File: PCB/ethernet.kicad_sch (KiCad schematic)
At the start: 32 parts, among them IC24 ENC28J60-I_SO, J6 74990101241, Y1 25MHz

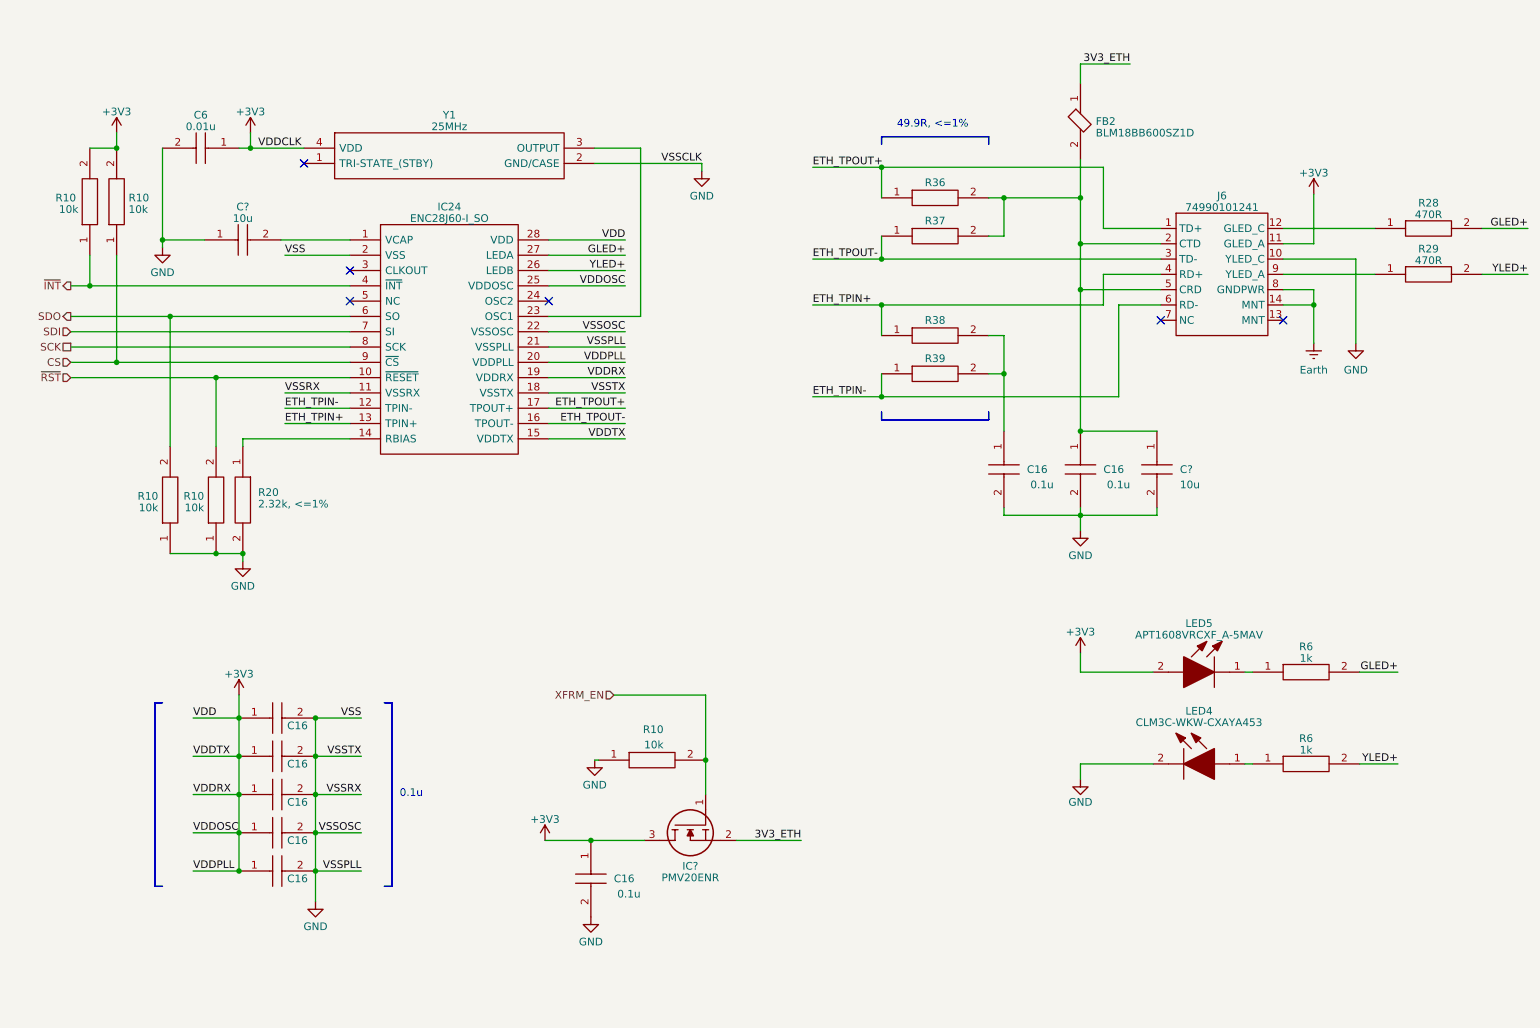
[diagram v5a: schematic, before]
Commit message: put pulldowns on unused OLED data lines and add a 510k to pin 13
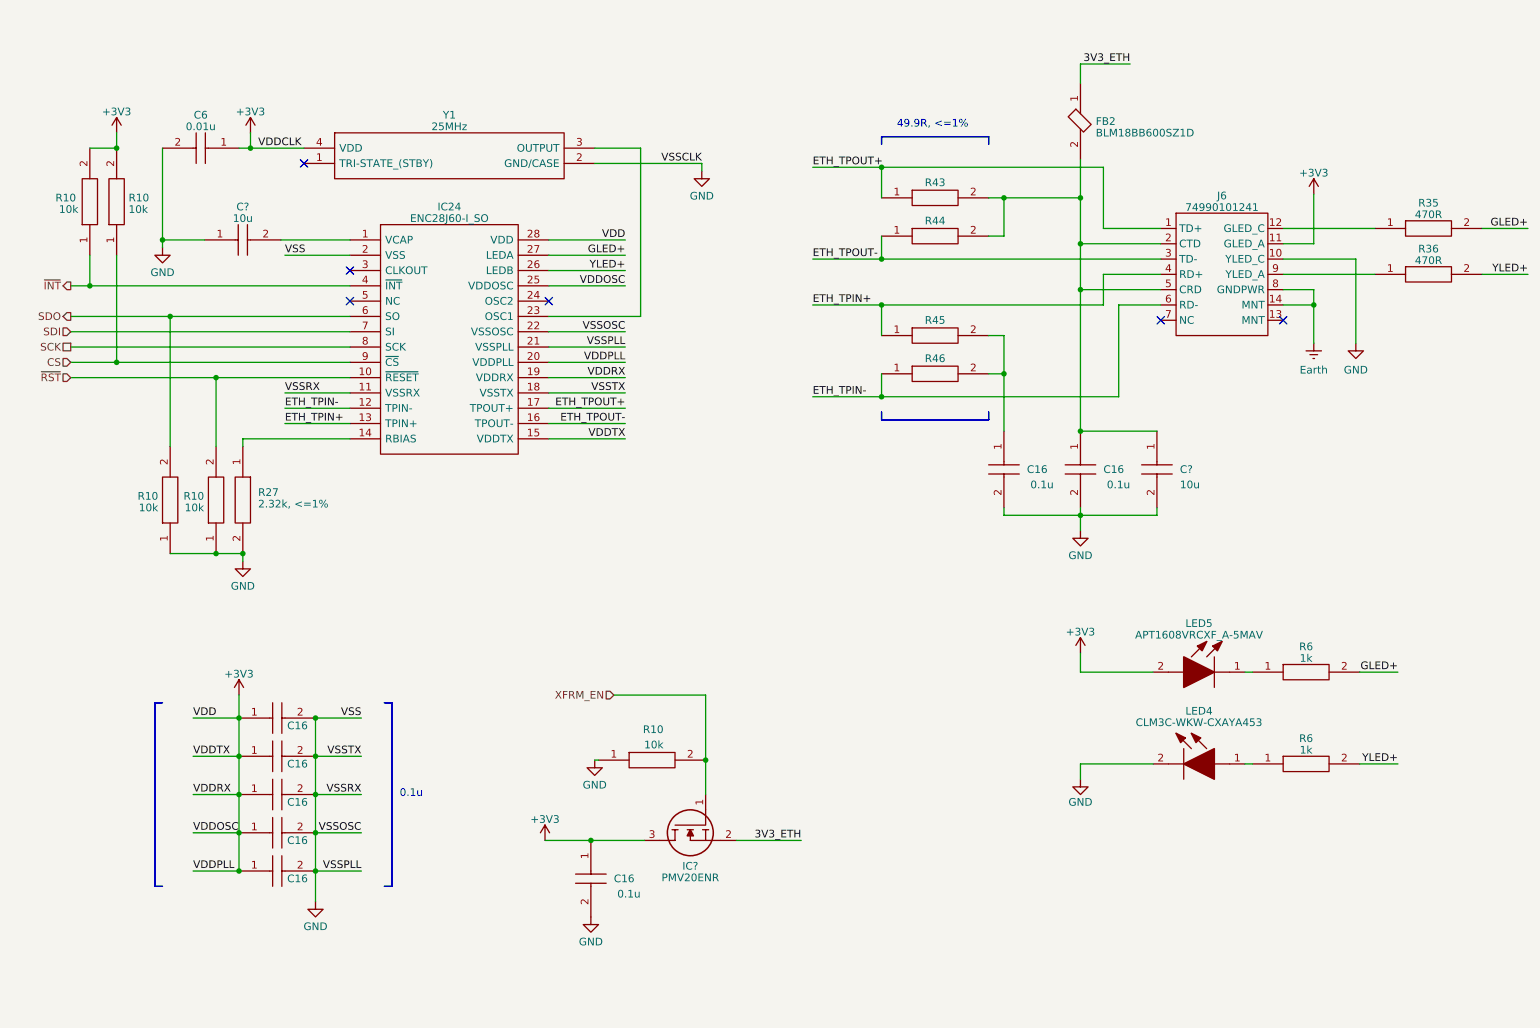
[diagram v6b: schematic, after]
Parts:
- renumbered R20 to R27, R28 to R35, R29 to R36, R36 to R43, R37 to R44, R38 to R45, R39 to R46
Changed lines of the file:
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@@
   (symbol (lib_id "SamacSys_Parts:ERJ-P06F2321V") (at 60.96 96.52 270) (unit 1)
     (in_bom yes) (on_board yes) (dnp no)
-    (property "Reference" "R20" (at 63.5 104.14 90)
+    (property "Reference" "R27" (at 63.5 104.14 90)
       (effects (font (size 1.27 1.27)) (justify left))
     )
@@
       (project "OroLink"
         (path "/e89dcd22-1250-4a5b-b778-1c95a0dd623d/52771c01-2e58-4900-abe5-411f688d020f"
-          (reference "R20") (unit 1)
-        )
-        (path "/e89dcd22-1250-4a5b-b778-1c95a0dd623d/7cebe953-3148-4b67-a6c9-1f2594261687"
-          (reference "R34") (unit 1)
+          (reference "R27") (unit 1)
+        )
+        (path "/e89dcd22-1250-4a5b-b778-1c95a0dd623d/7cebe953-3148-4b67-a6c9-1f2594261687"
+          (reference "R41") (unit 1)
         )
       )
@@
   (symbol (lib_id "SamacSys_Parts:RMCF0201FT49R9") (at 167.005 55.245 0) (unit 1)
     (in_bom yes) (on_board yes) (dnp no)
-    (property "Reference" "R36" (at 175.895 52.705 0)
+    (property "Reference" "R43" (at 175.895 52.705 0)
       (effects (font (size 1.27 1.27)))
     )
@@
       (project "OroLink"
         (path "/e89dcd22-1250-4a5b-b778-1c95a0dd623d/7cebe953-3148-4b67-a6c9-1f2594261687"
-          (reference "R36") (unit 1)
-        )
-        (path "/e89dcd22-1250-4a5b-b778-1c95a0dd623d/52771c01-2e58-4900-abe5-411f688d020f"
-          (reference "R22") (unit 1)
+          (reference "R43") (unit 1)
+        )
+        (path "/e89dcd22-1250-4a5b-b778-1c95a0dd623d/52771c01-2e58-4900-abe5-411f688d020f"
+          (reference "R29") (unit 1)
         )
       )
@@
         )
         (path "/e89dcd22-1250-4a5b-b778-1c95a0dd623d/52771c01-2e58-4900-abe5-411f688d020f"
-          (reference "R16") (unit 1)
-        )
-        (path "/e89dcd22-1250-4a5b-b778-1c95a0dd623d/7cebe953-3148-4b67-a6c9-1f2594261687"
-          (reference "R30") (unit 1)
+          (reference "R23") (unit 1)
+        )
+        (path "/e89dcd22-1250-4a5b-b778-1c95a0dd623d/7cebe953-3148-4b67-a6c9-1f2594261687"
+          (reference "R37") (unit 1)
         )
         (path "/e89dcd22-1250-4a5b-b778-1c95a0dd623d/dd173832-34f8-47c0-be66-f527d6e2d134"
@@
   (symbol (lib_id "SamacSys_Parts:RMCF0201FT49R9") (at 167.005 78.105 0) (unit 1)
     (in_bom yes) (on_board yes) (dnp no)
-    (property "Reference" "R38" (at 175.895 75.565 0)
+    (property "Reference" "R45" (at 175.895 75.565 0)
       (effects (font (size 1.27 1.27)))
     )
@@
       (project "OroLink"
         (path "/e89dcd22-1250-4a5b-b778-1c95a0dd623d/7cebe953-3148-4b67-a6c9-1f2594261687"
-          (reference "R38") (unit 1)
-        )
-        (path "/e89dcd22-1250-4a5b-b778-1c95a0dd623d/52771c01-2e58-4900-abe5-411f688d020f"
-          (reference "R24") (unit 1)
+          (reference "R45") (unit 1)
+        )
+        (path "/e89dcd22-1250-4a5b-b778-1c95a0dd623d/52771c01-2e58-4900-abe5-411f688d020f"
+          (reference "R31") (unit 1)
         )
       )
@@
         )
         (path "/e89dcd22-1250-4a5b-b778-1c95a0dd623d/52771c01-2e58-4900-abe5-411f688d020f"
-          (reference "R26") (unit 1)
-        )
-        (path "/e89dcd22-1250-4a5b-b778-1c95a0dd623d/7cebe953-3148-4b67-a6c9-1f2594261687"
-          (reference "R40") (unit 1)
+          (reference "R33") (unit 1)
+        )
+        (path "/e89dcd22-1250-4a5b-b778-1c95a0dd623d/7cebe953-3148-4b67-a6c9-1f2594261687"
+          (reference "R47") (unit 1)
         )
       )
@@
         )
         (path "/e89dcd22-1250-4a5b-b778-1c95a0dd623d/52771c01-2e58-4900-abe5-411f688d020f"
-          (reference "R27") (unit 1)
-        )
-        (path "/e89dcd22-1250-4a5b-b778-1c95a0dd623d/7cebe953-3148-4b67-a6c9-1f2594261687"
-          (reference "R41") (unit 1)
+          (reference "R34") (unit 1)
+        )
+        (path "/e89dcd22-1250-4a5b-b778-1c95a0dd623d/7cebe953-3148-4b67-a6c9-1f2594261687"
+          (reference "R48") (unit 1)
         )
       )
@@
   (symbol (lib_id "SamacSys_Parts:RMCF0201FT49R9") (at 167.005 84.455 0) (unit 1)
     (in_bom yes) (on_board yes) (dnp no)
-    (property "Reference" "R39" (at 175.895 81.915 0)
+    (property "Reference" "R46" (at 175.895 81.915 0)
       (effects (font (size 1.27 1.27)))
     )
@@
       (project "OroLink"
         (path "/e89dcd22-1250-4a5b-b778-1c95a0dd623d/7cebe953-3148-4b67-a6c9-1f2594261687"
-          (reference "R39") (unit 1)
-        )
-        (path "/e89dcd22-1250-4a5b-b778-1c95a0dd623d/52771c01-2e58-4900-abe5-411f688d020f"
-          (reference "R25") (unit 1)
+          (reference "R46") (unit 1)
+        )
+        (path "/e89dcd22-1250-4a5b-b778-1c95a0dd623d/52771c01-2e58-4900-abe5-411f688d020f"
+          (reference "R32") (unit 1)
         )
       )
@@
   (symbol (lib_id "SamacSys_Parts:AC0805FR-07470RL") (at 248.92 67.945 0) (unit 1)
     (in_bom yes) (on_board yes) (dnp no) (fields_autoplaced)
-    (property "Reference" "R29" (at 257.81 63.7159 0)
+    (property "Reference" "R36" (at 257.81 63.7159 0)
       (effects (font (size 1.27 1.27)))
     )
@@
       (project "OroLink"
         (path "/e89dcd22-1250-4a5b-b778-1c95a0dd623d/52771c01-2e58-4900-abe5-411f688d020f"
-          (reference "R29") (unit 1)
-        )
-        (path "/e89dcd22-1250-4a5b-b778-1c95a0dd623d/7cebe953-3148-4b67-a6c9-1f2594261687"
-          (reference "R43") (unit 1)
+          (reference "R36") (unit 1)
+        )
+        (path "/e89dcd22-1250-4a5b-b778-1c95a0dd623d/7cebe953-3148-4b67-a6c9-1f2594261687"
+          (reference "R50") (unit 1)
         )
       )
@@
         )
         (path "/e89dcd22-1250-4a5b-b778-1c95a0dd623d/52771c01-2e58-4900-abe5-411f688d020f"
-          (reference "R21") (unit 1)
-        )
-        (path "/e89dcd22-1250-4a5b-b778-1c95a0dd623d/7cebe953-3148-4b67-a6c9-1f2594261687"
-          (reference "R35") (unit 1)
+          (reference "R28") (unit 1)
+        )
+        (path "/e89dcd22-1250-4a5b-b778-1c95a0dd623d/7cebe953-3148-4b67-a6c9-1f2594261687"
+          (reference "R42") (unit 1)
         )
         (path "/e89dcd22-1250-4a5b-b778-1c95a0dd623d/dd173832-34f8-47c0-be66-f527d6e2d134"
@@
         )
         (path "/e89dcd22-1250-4a5b-b778-1c95a0dd623d/52771c01-2e58-4900-abe5-411f688d020f"
-          (reference "R19") (unit 1)
-        )
-        (path "/e89dcd22-1250-4a5b-b778-1c95a0dd623d/7cebe953-3148-4b67-a6c9-1f2594261687"
-          (reference "R33") (unit 1)
+          (reference "R26") (unit 1)
+        )
+        (path "/e89dcd22-1250-4a5b-b778-1c95a0dd623d/7cebe953-3148-4b67-a6c9-1f2594261687"
+          (reference "R40") (unit 1)
         )
         (path "/e89dcd22-1250-4a5b-b778-1c95a0dd623d/dd173832-34f8-47c0-be66-f527d6e2d134"
@@
   (symbol (lib_id "SamacSys_Parts:AC0805FR-07470RL") (at 248.92 60.325 0) (unit 1)
     (in_bom yes) (on_board yes) (dnp no) (fields_autoplaced)
-    (property "Reference" "R28" (at 257.81 56.0959 0)
+    (property "Reference" "R35" (at 257.81 56.0959 0)
       (effects (font (size 1.27 1.27)))
     )
@@
       (project "OroLink"
         (path "/e89dcd22-1250-4a5b-b778-1c95a0dd623d/52771c01-2e58-4900-abe5-411f688d020f"
-          (reference "R28") (unit 1)
-        )
-        (path "/e89dcd22-1250-4a5b-b778-1c95a0dd623d/7cebe953-3148-4b67-a6c9-1f2594261687"
-          (reference "R42") (unit 1)
+          (reference "R35") (unit 1)
+        )
+        (path "/e89dcd22-1250-4a5b-b778-1c95a0dd623d/7cebe953-3148-4b67-a6c9-1f2594261687"
+          (reference "R49") (unit 1)
         )
       )
@@
         )
         (path "/e89dcd22-1250-4a5b-b778-1c95a0dd623d/52771c01-2e58-4900-abe5-411f688d020f"
-          (reference "R17") (unit 1)
-        )
-        (path "/e89dcd22-1250-4a5b-b778-1c95a0dd623d/7cebe953-3148-4b67-a6c9-1f2594261687"
-          (reference "R31") (unit 1)
+          (reference "R24") (unit 1)
+        )
+        (path "/e89dcd22-1250-4a5b-b778-1c95a0dd623d/7cebe953-3148-4b67-a6c9-1f2594261687"
+          (reference "R38") (unit 1)
         )
         (path "/e89dcd22-1250-4a5b-b778-1c95a0dd623d/dd173832-34f8-47c0-be66-f527d6e2d134"
@@
         )
         (path "/e89dcd22-1250-4a5b-b778-1c95a0dd623d/52771c01-2e58-4900-abe5-411f688d020f"
-          (reference "R18") (unit 1)
-        )
-        (path "/e89dcd22-1250-4a5b-b778-1c95a0dd623d/7cebe953-3148-4b67-a6c9-1f2594261687"
-          (reference "R32") (unit 1)
+          (reference "R25") (unit 1)
+        )
+        (path "/e89dcd22-1250-4a5b-b778-1c95a0dd623d/7cebe953-3148-4b67-a6c9-1f2594261687"
+          (reference "R39") (unit 1)
         )
         (path "/e89dcd22-1250-4a5b-b778-1c95a0dd623d/dd173832-34f8-47c0-be66-f527d6e2d134"
@@
   (symbol (lib_id "SamacSys_Parts:RMCF0201FT49R9") (at 167.005 61.595 0) (unit 1)
     (in_bom yes) (on_board yes) (dnp no)
-    (property "Reference" "R37" (at 175.895 59.055 0)
+    (property "Reference" "R44" (at 175.895 59.055 0)
       (effects (font (size 1.27 1.27)))
     )
@@
       (project "OroLink"
         (path "/e89dcd22-1250-4a5b-b778-1c95a0dd623d/7cebe953-3148-4b67-a6c9-1f2594261687"
-          (reference "R37") (unit 1)
-        )
-        (path "/e89dcd22-1250-4a5b-b778-1c95a0dd623d/52771c01-2e58-4900-abe5-411f688d020f"
-          (reference "R23") (unit 1)
-        )
-      )
+          (reference "R44") (unit 1)
+        )
+        (path "/e89dcd22-1250-4a5b-b778-1c95a0dd623d/52771c01-2e58-4900-abe5-411f688d020f"
+          (reference "R30") (unit 1)
+        )
+      )

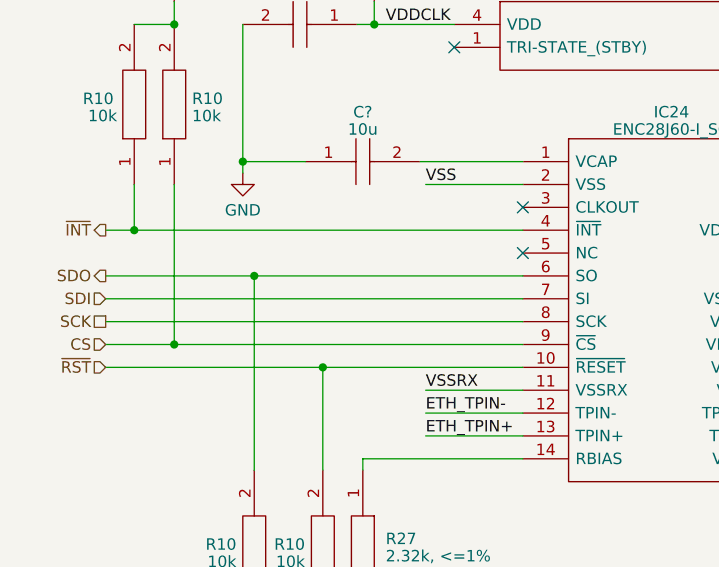
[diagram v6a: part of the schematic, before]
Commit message: add debug pins to signal lines (closes #16)
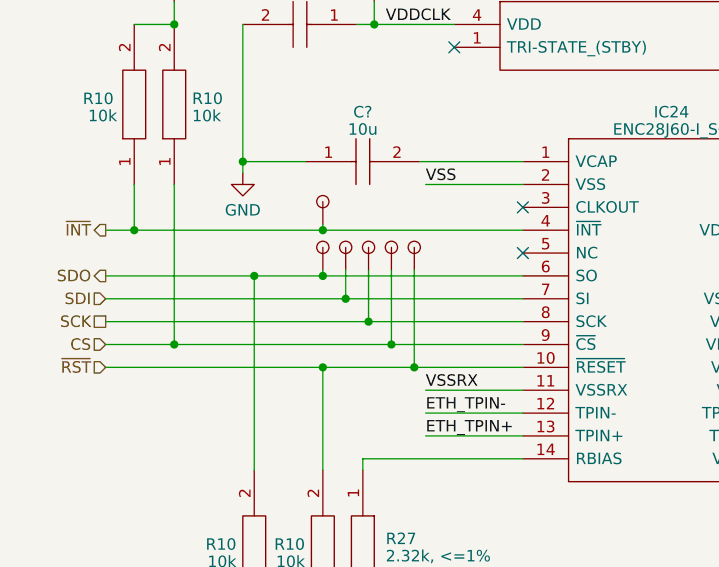
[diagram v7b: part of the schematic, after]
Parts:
- added DBG5 (x6): ~, Oro Footprints:DebugPin, symbol Oro:DebugPin
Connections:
- net CS: now also DBG5.1
- net SCK: now also DBG5.1
- net SDI: now also DBG5.1
- net SDO: now also DBG5.1
- net ~{INT}: now also DBG5.1
- net ~{RST}: now also DBG5.1

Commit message: replace 49.9R resistors with larger package (closes #20)
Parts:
- R43, R44, R45, R46: footprint RESC0603X26N -> RESC1005X35N; symbol SamacSys_Parts:RMCF0201FT49R9 -> SamacSys_Parts:RT0402FRE0749R9L; Height 0.26 -> 0.35; Manufacturer_Name Stackpole Electronics, Inc. -> KEMET; Manufacturer_Part_Number RMCF0201FT49R9 -> RT0402FRE0749R9L; Mouser Part Number 708-RMCF0201FT49R9 -> 603-RT0402FRE0749R9L; Mouser Price/Stock https://www.mouser.de/ProductDetail/SEI-Stackpole/RMCF0201F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 -> https://www.mouser.co.uk/ProductDetail/YAGEO/RT0402FRE0749R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
